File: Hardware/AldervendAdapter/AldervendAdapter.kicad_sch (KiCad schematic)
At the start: 0 parts

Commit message: Bump MVD
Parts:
- added H101, H102, H103, H104: MountingHole, MountingHole:MountingHole_4.3mm_M4, symbol Mechanical:MountingHole
- added J101: MDB_IN, Connector_Molex:Molex_Mini-Fit_Jr_5569-06A2_2x03_P4.20mm_Horizontal, symbol Connector_Generic:Conn_02x03_Top_Bottom
- added J102: MDB_OUT, Connector_Molex:Molex_Mini-Fit_Jr_5569-06A2_2x03_P4.20mm_Horizontal, symbol Connector_Generic:Conn_02x03_Top_Bottom
- added U101: ESP32-WROOM-32D, RF_Module:ESP32-WROOM-32D, symbol RF_Module:ESP32-WROOM-32D
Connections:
- new net: U101.1 (GND), U101.15 (GND), U101.38 (GND), U101.39 (GND)

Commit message: Add some sch work
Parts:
- added Q101: 2N3904, Package_TO_SOT_SMD:SOT-323_SC-70, symbol Transistor_BJT:2N3904
- added R101: R_Small, Resistor_SMD:R_0805_2012Metric, symbol Device:R_Small
- added R102: 1k, Resistor_SMD:R_0805_2012Metric, symbol Device:R_Small
- J101: value MDB_IN -> MDB_PUBLISHER
- J102: value MDB_OUT -> MDB_SUBSCRIBER; now not fitted
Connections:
- net GND: now reaches U101.1 (GND), U101.15 (GND), U101.38 (GND), U101.39 (GND)
- net GND: now also J101.2 (Pin_2), J101.6 (Pin_6), J102.2 (Pin_2), J102.6 (Pin_6), R102.2
- net +3.3V: now reaches U101.2 (VDD)
- net +24V: now reaches J101.1 (Pin_1)
- net +24V: now also J102.1 (Pin_1)
- net MDB_RXD: now reaches J101.4 (Pin_4)
- net MDB_RXD: now also J102.4 (Pin_4)
- net MDB_TXD: now reaches J101.5 (Pin_5)
- net MDB_TXD: now also J102.5 (Pin_5)
- no-connect marks 0 -> 2
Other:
- note added: "((5 volts) − (1.15 volts)) / (5 milliamperes) = 770 Ω"
- note added: "VERIFY FOOTPRINT"
- note added: "use Broadcom ACPL-064L-500E"
- moved on the sheet: J101

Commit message: Enough free work for today
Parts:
- removed U101: ESP32-WROOM-32D, RF_Module:ESP32-WROOM-32D, symbol RF_Module:ESP32-WROOM-32D
- added C101: 680uF, Capacitor_SMD:C_Elec_10x10.2, symbol Device:C
- added C102: 220uF, Capacitor_SMD:C_Elec_6.3x5.4, symbol Device:C_Small
- added D101: SS34, Diode_SMD:D_SMA, symbol Diode:SS34
- added L101: L, Inductor_SMD:L_6.3x6.3_H3, symbol Device:L
- added R103: 0R, Resistor_SMD:R_0805_2012Metric, symbol Device:R_Small
- added U101, U102: TLP2310, Package_SO:SO-5-6_4.55x3.7mm_P1.27mm, symbol Isolator:TLP2310
- added U103: ESP32-C6-MINI-1, RF_Module:ESP32-C6-MINI-1, symbol RF_Module:ESP32-C6-MINI-1
- added U104: LM2596S-5, Package_TO_SOT_SMD:TO-263-5_TabPin3, symbol Regulator_Switching:LM2596S-5
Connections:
- net +24V: now also C101.1, U104.1 (VIN)
- net +3.3V: now also U103.3 (3V3)
- net GND: now also C101.2, C102.2, D101.2 (A), R103.2, U103.1 (GND), U103.11 (GND), U103.14 (GND), U103.2 (GND), U103.36 (GND), U103.37 (GND), U103.38 (GND), U103.39 (GND), U103.40 (GND), U103.41 (GND), U103.42 (GND), U103.43 (GND), U103.44 (GND), U103.45 (GND), U103.46 (GND), U103.47 (GND), U103.48 (GND), U103.49 (GND), U103.50 (GND), U103.51 (GND), U103.52 (GND), U103.53 (GND), U104.3 (GND)
- new net: D101.1 (K), L101.1, U104.2 (OUT)
- new net: C102.1, L101.2, U104.4 (FB)
- new net: R103.1, U104.5 (~{ON}/OFF)
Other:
- note added: "MDB Spec https://www.namanow.org/wp-content/uploads/Multi-Drop-Bus-and-Internal-Communication-Protocol.pdf"

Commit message: Make aldervon logo
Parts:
- added U105: ~, symbol Aldervon:AldervonLogo
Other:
- company: Aldervon Systems -> (none)
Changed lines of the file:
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@@
 		(title "AldervendAdapter")
 		(rev "${REVISION}")
-		(company "Aldervon Systems")
 	)
 	(text "((5 volts) − (1.15 volts)) / (5 milliamperes)\n= 770 Ω\n"
@@
 					(unit 1)
 				)
+			)
+		)
+	)
+	(symbol
+		(lib_id "Aldervon:AldervonLogo")
+		(at 177.8 181.61 0)
+		(unit 1)
+		(exclude_from_sim no)
+		(in_bom yes)
+		(on_board yes)
+		(dnp no)
+		(fields_autoplaced yes)
+		(property "Reference" "U105"
+			(at 189.23 175.514 0)
+			(effects
+				(font
+					(size 1.27 1.27)
+				)
+				(hide yes)
+			)
+		)
+		(property "Value" "~"
+			(at 189.23 178.054 0)
+			(effects
+				(font
+					(size 1.27 1.27)
+				)
+				(hide yes)
+			)
+		)
+		(property "Footprint" ""
+			(at 177.8 181.61 0)
+			(effects
+				(font
+					(size 1.27 1.27)
+				)
+				(hide yes)
+			)
+		)
+		(property "Datasheet" ""
+			(at 177.8 181.61 0)
+			(effects
+				(font
+					(size 1.27 1.27)
+				)
+				(hide yes)
+			)
+		)
+		(property "Description" ""
+			(at 177.8 181.61 0)
+			(effects
+				(font
+					(size 1.27 1.27)
+				)
+				(hide yes)
+			)
+		)
+		(instances
+			(project ""
+				(path "/894f620e-3404-4a40-a2a7-513bc1d5f99b"
+					(reference "U105")
+					(unit 1)
+				)

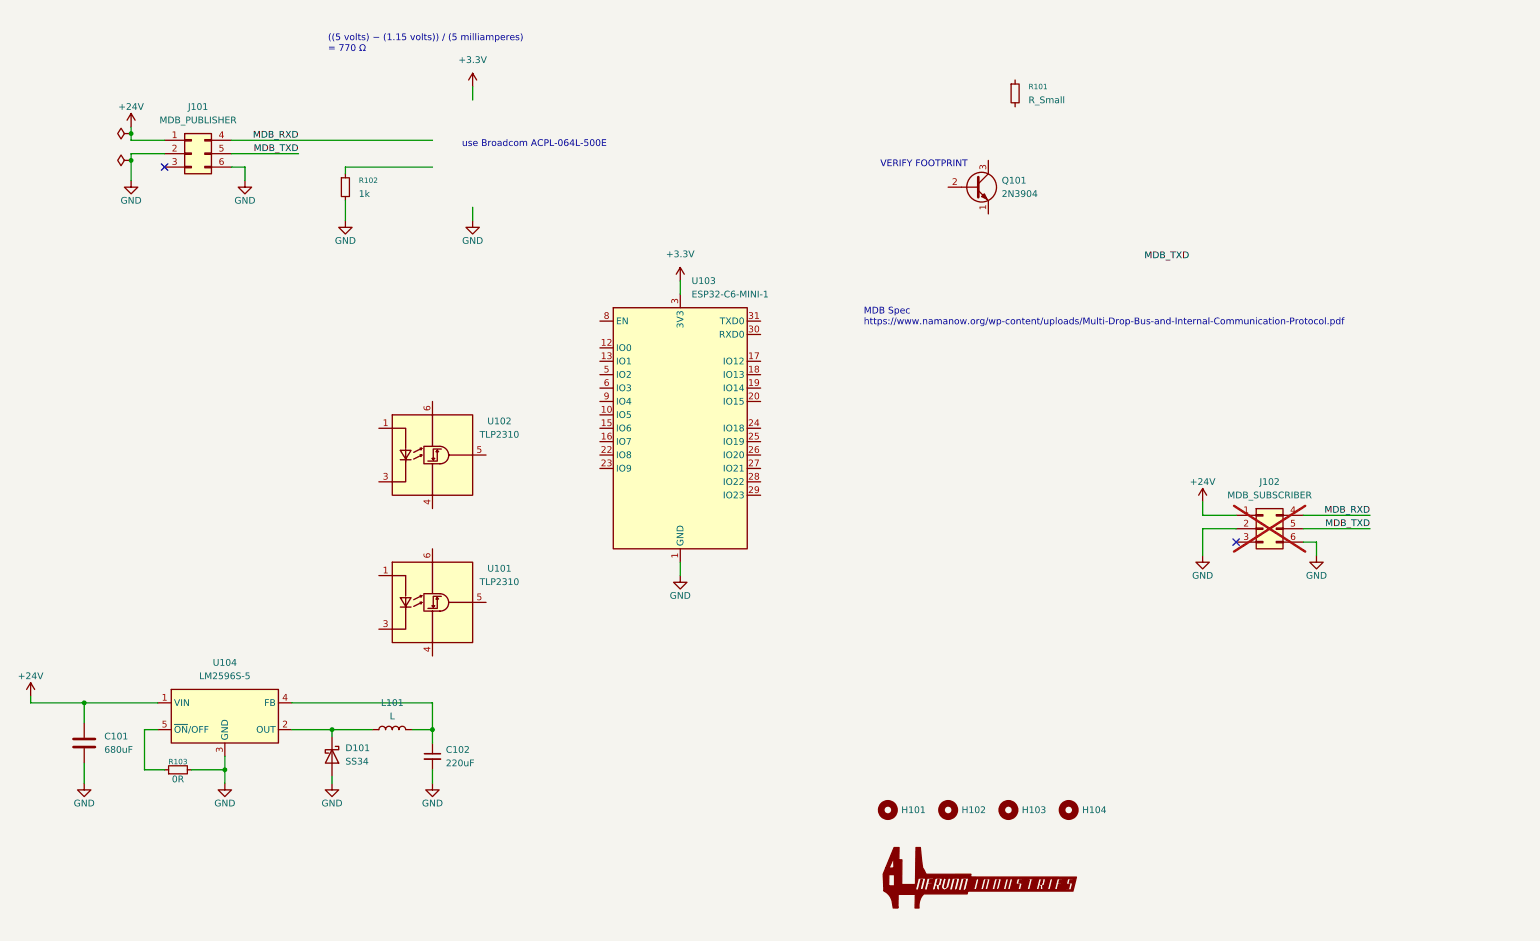
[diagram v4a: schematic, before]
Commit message: Settle in on a vrm and other optos
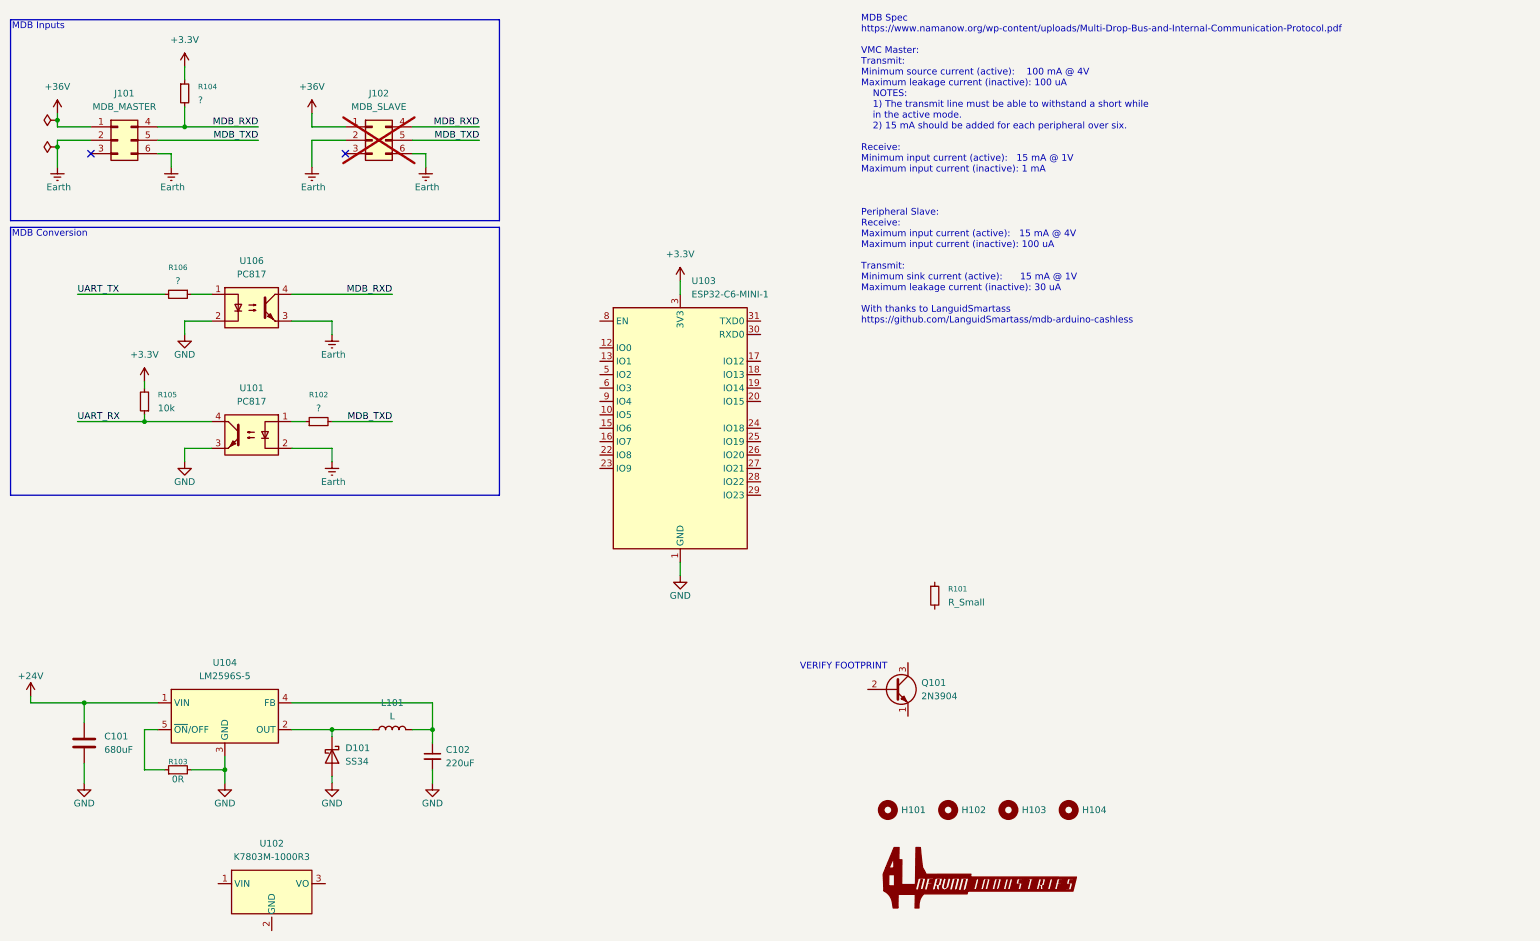
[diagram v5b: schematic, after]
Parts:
- removed U101, U102: TLP2310, Package_SO:SO-5-6_4.55x3.7mm_P1.27mm, symbol Isolator:TLP2310
- added R104, R106: ?, Resistor_SMD:R_0805_2012Metric, symbol Device:R_Small
- added R105: 10k, Resistor_SMD:R_0805_2012Metric, symbol Device:R_Small
- added U101, U106: PC817, Package_DIP:DIP-4_W7.62mm_SMDSocket_SmallPads, symbol Isolator:PC817
- added U102: K7803M-1000R3, symbol Aldervon:K7803M-1000R3
- J101: value MDB_PUBLISHER -> MDB_MASTER
- J102: value MDB_SUBSCRIBER -> MDB_SLAVE
- R102: value 1k -> ?
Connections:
- net +24V: no longer J101.1 (Pin_1), J102.1 (Pin_1)
- net +3.3V: now also R104.1, R105.2
- net GND: now also U101.3, U106.2; no longer J101.2 (Pin_2), J101.6 (Pin_6), J102.2 (Pin_2), J102.6 (Pin_6), R102.2
- net MDB_RXD: now also R104.2, U106.4
- net MDB_TXD: now also R102.2
- net at R102.1: now also U101.1
- new net: R106.1, U106.1
- new net +36V: J101.1 (Pin_1), J102.1 (Pin_1)
- new net Earth: J101.2 (Pin_2), J101.6 (Pin_6), J102.2 (Pin_2), J102.6 (Pin_6), U101.2, U106.3
- new net UART_RX: R105.1, U101.4
- new net UART_TX: R106.2
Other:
- note added: "MDB Conversion"
- note added: "MDB Inputs"
- note added: "MDB Spec https://www.namanow.org/wp-content/uploads/Multi-Drop-Bus-and-Internal-Communication-Protocol.pdf VMC Master: Transmit: Minimum source current (active): 100 mA @ 4V Maximum leakage current (inactive): 100 uA NOTES: 1) The transmit line must be able to withstand a short while in the active mode. 2) 15 mA should be added for each peripheral over six. Receive: Minimum input current (active)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"
- note removed: "((5 volts) − (1.15 volts)) / (5 milliamperes) = 770 Ω"
- note removed: "MDB Spec https://www.namanow.org/wp-content/uploads/Multi-Drop-Bus-and-Internal-Communication-Protocol.pdf"
- note removed: "use Broadcom ACPL-064L-500E"
- moved on the sheet: J101, J102, Q101, R101

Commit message: Finish schematic
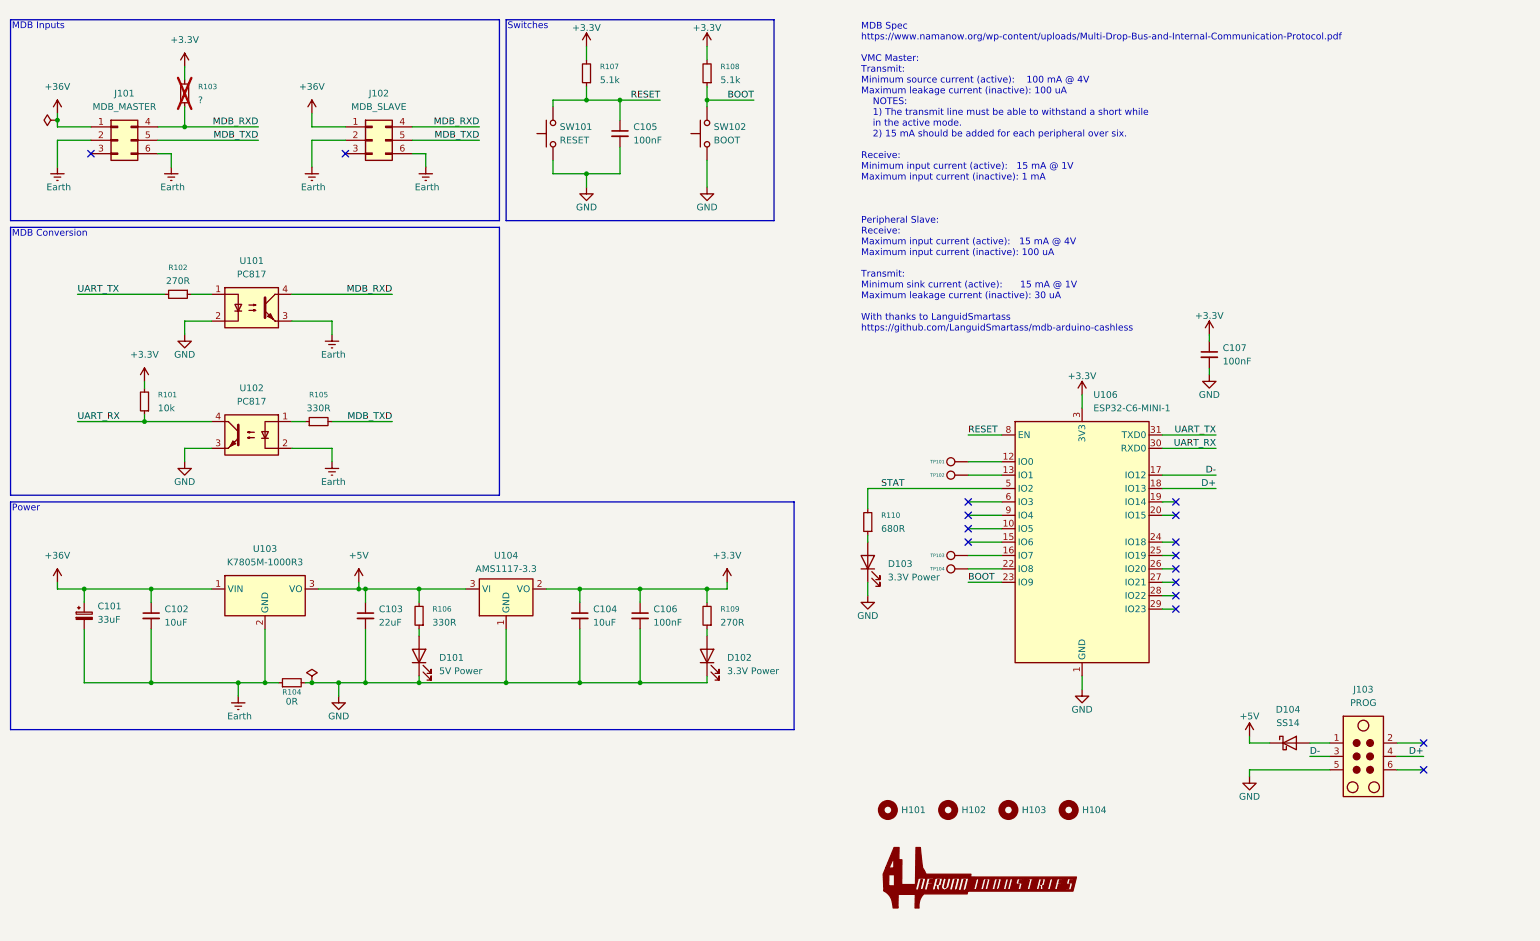
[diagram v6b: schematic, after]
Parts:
- removed C101: 680uF, Capacitor_SMD:C_Elec_10x10.2, symbol Device:C
- removed D101: SS34, Diode_SMD:D_SMA, symbol Diode:SS34
- removed L101: L, Inductor_SMD:L_6.3x6.3_H3, symbol Device:L
- removed Q101: 2N3904, Package_TO_SOT_SMD:SOT-323_SC-70, symbol Transistor_BJT:2N3904
- removed R101: R_Small, Resistor_SMD:R_0805_2012Metric, symbol Device:R_Small
- removed R103: 0R, Resistor_SMD:R_0805_2012Metric, symbol Device:R_Small
- removed U102: K7803M-1000R3, symbol Aldervon:K7803M-1000R3
- removed U104: LM2596S-5, Package_TO_SOT_SMD:TO-263-5_TabPin3, symbol Regulator_Switching:LM2596S-5
- added C101: 33uF, Capacitor_SMD:C_Elec_5x5.4, symbol Device:C_Polarized_Small
- added C103: 22uF, Capacitor_SMD:C_Elec_6.3x5.4, symbol Device:C_Small
- added C104: 10uF, Capacitor_SMD:C_0805_2012Metric, symbol Device:C_Small
- added C105, C106, C107: 100nF, Capacitor_SMD:C_0805_2012Metric, symbol Device:C_Small
- added D101: 5V Power, LED_SMD:LED_0805_2012Metric, symbol Device:LED
- added D102, D103: 3.3V Power, LED_SMD:LED_0805_2012Metric, symbol Device:LED
- added D104: SS14, Diode_SMD:D_SMA, symbol Diode:SS14
- added J103: PROG, Connector:Tag-Connect_TC2030-IDC-FP_2x03_P1.27mm_Vertical, symbol Connector:TC2030
- added R104: 0R, Resistor_SMD:R_0805_2012Metric, symbol Device:R_Small
- added R106: 330R, Resistor_SMD:R_0805_2012Metric, symbol Device:R_Small
- added R107, R108: 5.1k, Resistor_SMD:R_0805_2012Metric, symbol Device:R_Small
- added R109: 270R, Resistor_SMD:R_0805_2012Metric, symbol Device:R_Small
- added R110: 680R, Resistor_SMD:R_0805_2012Metric, symbol Device:R_Small
- added SW101: RESET, Button_Switch_SMD:SW_Push_1P1T_NO_CK_KMR2, symbol Switch:SW_Push
- added SW102: BOOT, Button_Switch_SMD:SW_Push_1P1T_NO_CK_KMR2, symbol Switch:SW_Push
- added TP101, TP102, TP103, TP104: TestPoint, TestPoint:TestPoint_Pad_2.0x2.0mm, symbol Connector:TestPoint
- added U103: K7805M-1000R3, symbol Aldervon:K7805M-1000R3
- added U104: AMS1117-3.3, Package_TO_SOT_SMD:SOT-223-3_TabPin2, symbol Regulator_Linear:AMS1117-3.3
- C102: value 220uF -> 10uF; footprint Capacitor_SMD:C_Elec_6.3x5.4 -> Capacitor_SMD:C_0805_2012Metric; LCSC# C72494 -> C440198
- J102: now fitted
- R101: renamed from R105; LCSC# (none) -> C84376
- R102: renamed from R106; value ? -> 270R; LCSC# (none) -> C17590
- R103: renamed from R104; now not fitted
- R105: renamed from R102; value ? -> 330R; LCSC# (none) -> C17630
- renumbered U106 to U101, U101 to U102, U103 to U106
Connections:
- net +3.3V: now also C104.1, C106.1, C107.1, R107.2, R108.2, R109.2, U104.2 (VO)
- net +36V: now also C102.1, C101.1, U103.1 (VIN)
- net Earth: now also C102.2, C101.2, R104.1, U103.2 (GND)
- net GND: now also C103.2, C104.2, C105.2, C106.2, C107.2, D101.1 (K), D102.1 (K), D103.1 (K), J103.5, R104.2, SW101.1, SW102.1, U104.1 (GND); no longer C102.2
- net UART_RX: now also U106.30 (RXD0)
- net UART_TX: now also U106.31 (TXD0)
- net at U106.12 (IO0): now also TP101.1
- net at U106.13 (IO1): now also TP102.1
- net at U106.16 (IO7): now also TP103.1
- net D-: now reaches U106.17 (IO12)
- net D-: now also J103.3
- net D+: now reaches U106.18 (IO13)
- net D+: now also J103.4
- net at U106.22 (IO8): now also TP104.1
- net BOOT: now reaches U106.23 (IO9)
- net BOOT: now also R108.1, SW102.2
- net STAT: now reaches U106.5 (IO2)
- net STAT: now also R110.2
- net RESET: now reaches U106.8 (EN)
- net RESET: now also C105.1, R107.1, SW101.2
- new net: D103.2 (A), R110.1
- new net: D101.2 (A), R106.1
- new net: D102.2 (A), R109.1
- new net: D104.2 (A), J103.1
- new net +5V: C103.1, D104.1 (K), R106.2, U103.3 (VO), U104.3 (VI)
- no-connect marks 2 -> 16
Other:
- note added: "Power"
- note added: "Switches"
- note removed: "VERIFY FOOTPRINT"
- moved on the sheet: U106

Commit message: Add all but finishing touches
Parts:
- D103: value 3.3V Power -> Stat
- U103: footprint (none) -> Aldervon:K7805M-1000R3
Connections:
- net Earth: now also D101.1 (K)
- net GND: no longer D101.1 (K)
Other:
- moved on the sheet: C103, D101, R104, R106

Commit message: Find some replacement parts for standard assembly
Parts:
- C101: LCSC# C74622 -> C27784
- C103: footprint Capacitor_SMD:C_Elec_6.3x5.4 -> Capacitor_SMD:C_Elec_4x5.4; LCSC# C72494 -> C3356
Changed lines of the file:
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@@
 			)
 		)
-		(property "Footprint" "Capacitor_SMD:C_Elec_6.3x5.4"
+		(property "Footprint" "Capacitor_SMD:C_Elec_4x5.4"
 			(at 93.98 125.73 0)
 			(effects
@@
 			)
 		)
-		(property "LCSC#" "C72494"
+		(property "LCSC#" "C3356"
 			(at 93.98 125.73 0)
 			(effects
@@
 			)
 		)
-		(property "LCSC#" "C74622"
+		(property "LCSC#" "C27784"
 			(at 26.67 125.73 0)
 			(effects
